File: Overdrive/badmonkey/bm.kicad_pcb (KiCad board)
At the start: 2 copper layers, 59.4 x 40 mm, 37 parts, among them J1 Conn_01x04_Pin, Q1 2N3904, U1 4558, U2 4558

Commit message: missing files
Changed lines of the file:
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@@
         (effects (font (size 1 1) (thickness 0.15)))
     )
-    (fp_text value "10u" (at 1.25 3.75) (layer "F.Fab")
+    (fp_text value "10u" (at -1.45 2.75) (layer "F.SilkS")
         (effects (font (size 1 1) (thickness 0.15)))
     )
-    (fp_text user "${REFERENCE}" (at 1.25 0) (layer "F.Fab")
+    (fp_text user "${REFERENCE}" (at 1.25 0) (layer "F.Fab") hide
         (effects (font (size 1 1) (thickness 0.15)))
     )

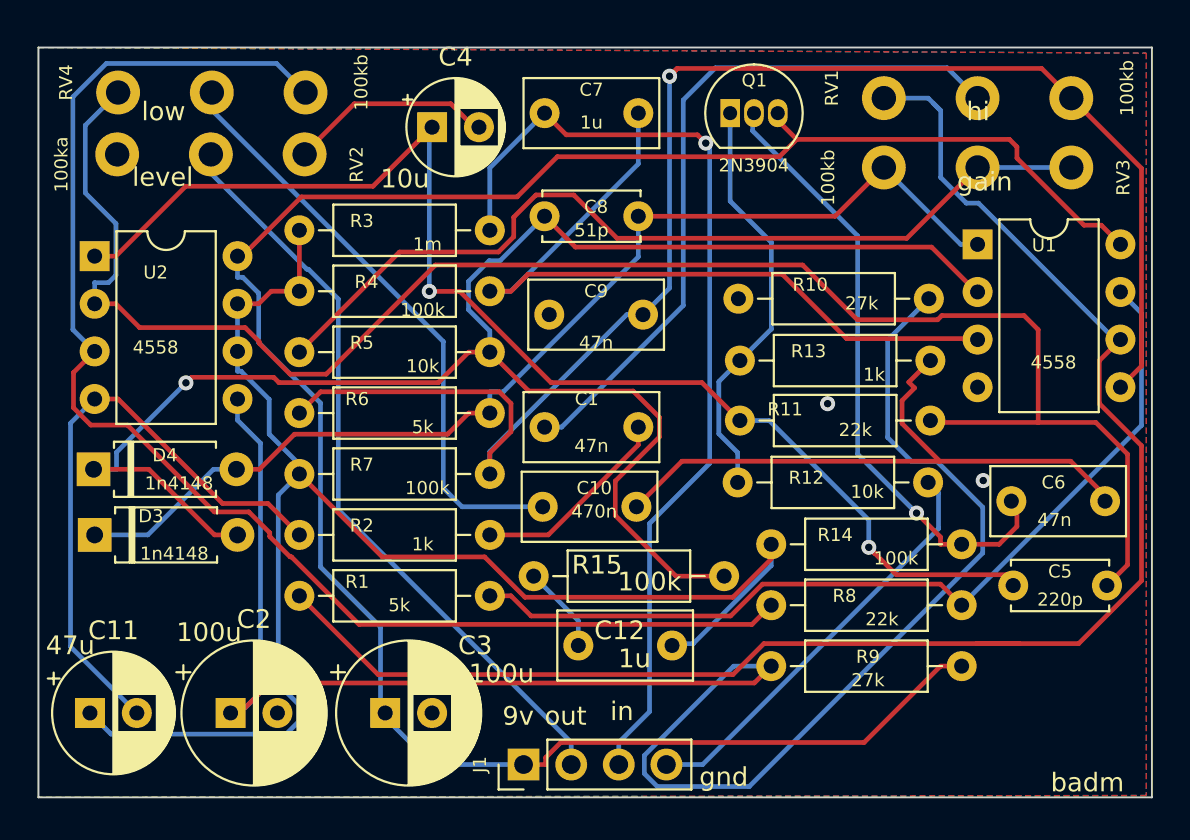
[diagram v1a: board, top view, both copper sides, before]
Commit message: fix to badmonkey -- pedal works but the schematic this was based on does not seem right.   There's a voltage offset on the input when engaged, and this messes with it in the pedal chain.
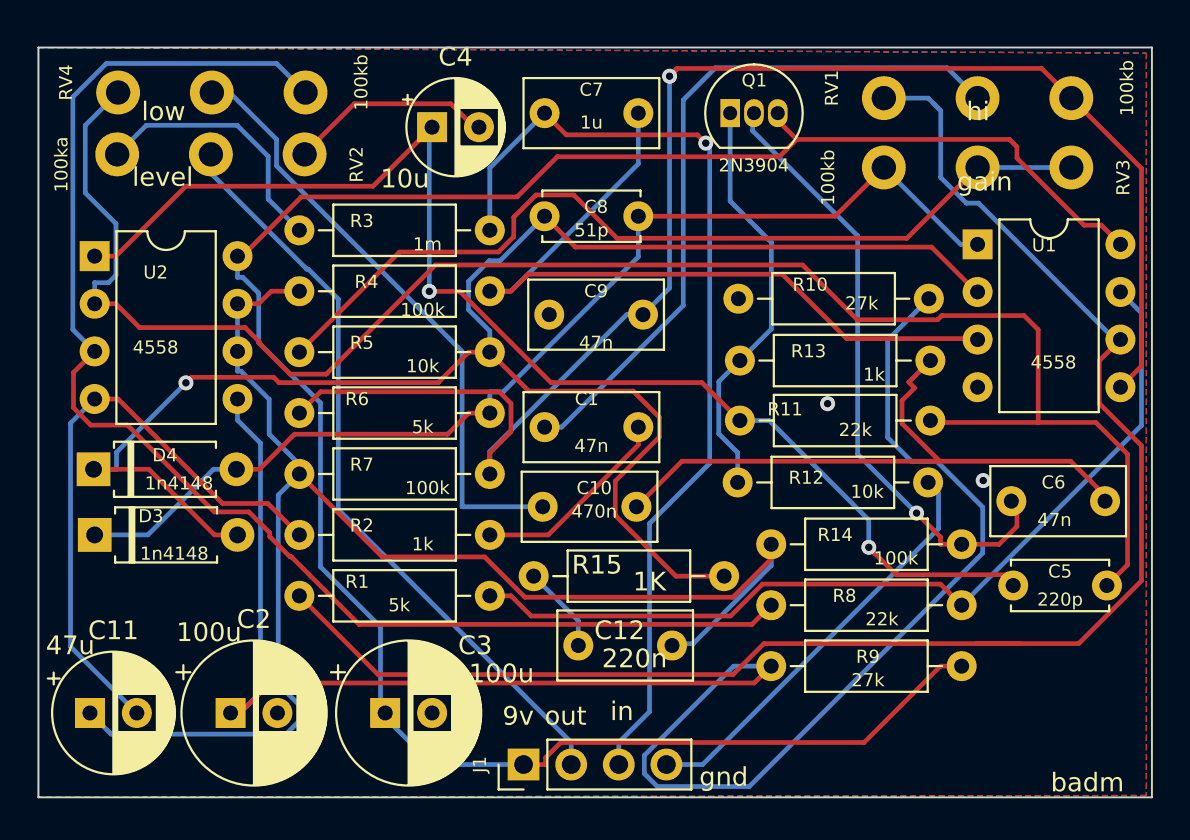
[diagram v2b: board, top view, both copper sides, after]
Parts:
- C12: value 1u -> 220n
- R15: value 100k -> 1K
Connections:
- R3 pad 1: vb -> GND
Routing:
- net GND: track 55.6 -> 69.6 mm
- net vb: track 81.1 -> 77.8 mm
- net Net-(C10-Pad1): track 32.1 -> 32.6 mm
